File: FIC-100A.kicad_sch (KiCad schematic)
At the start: 0 parts

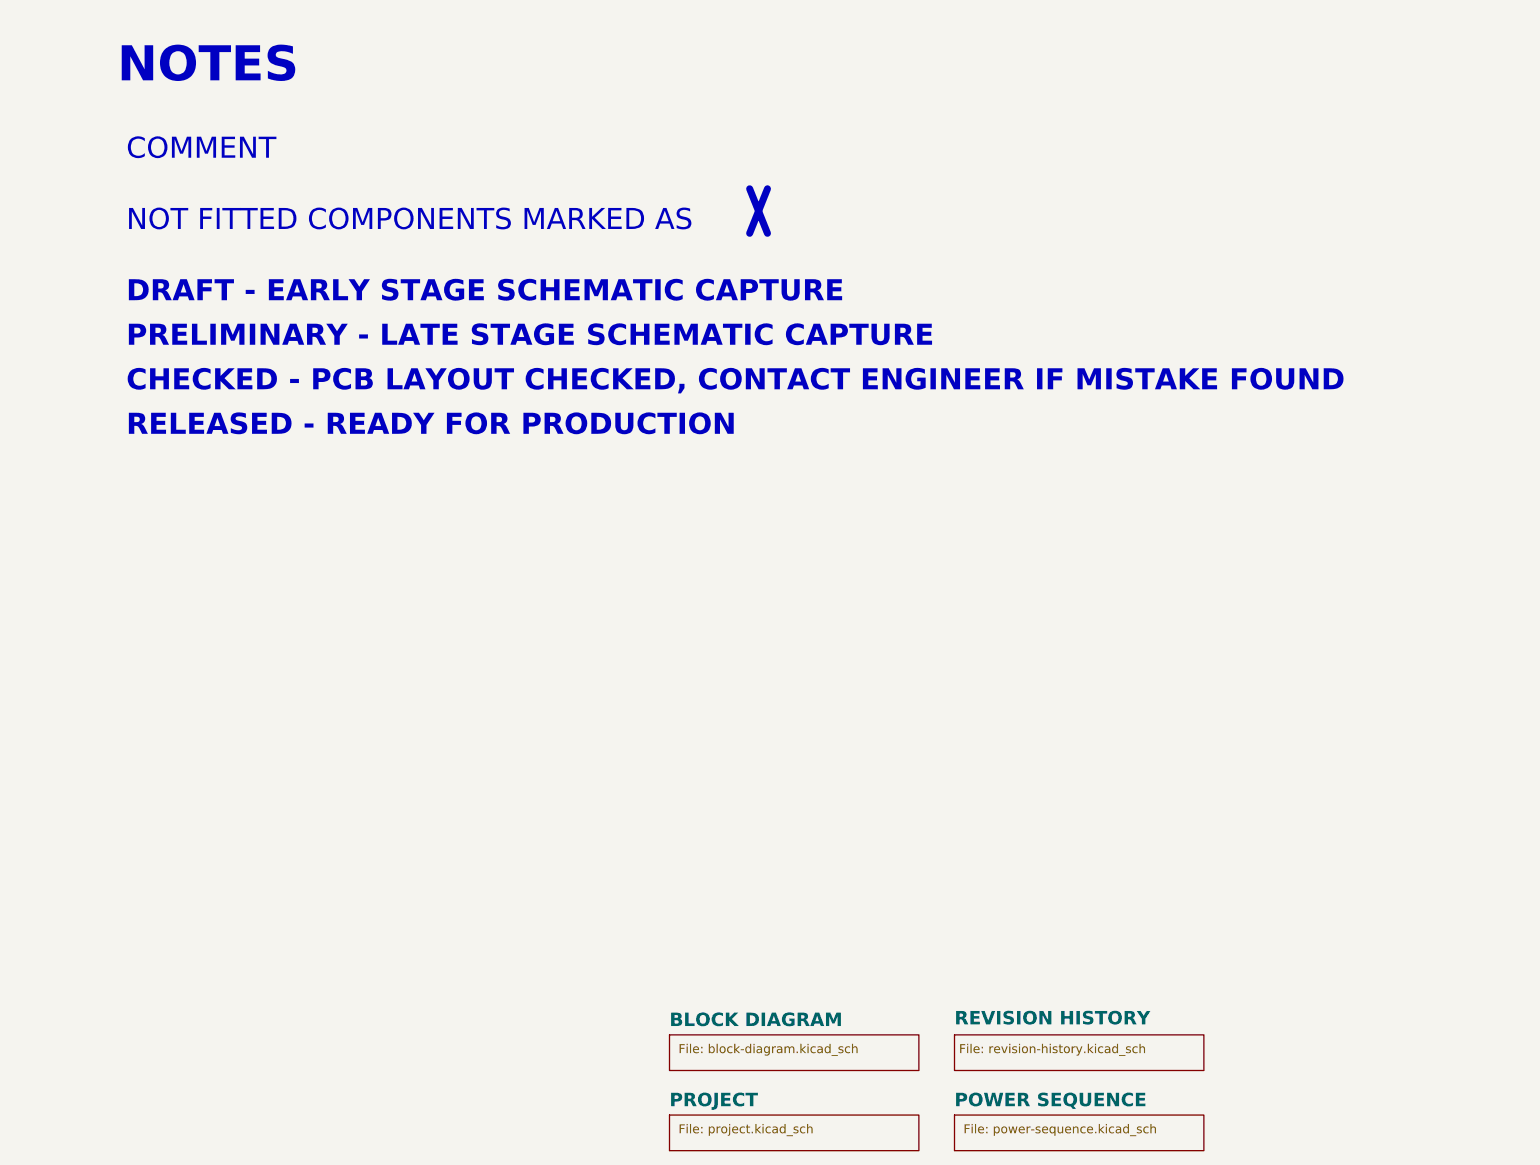
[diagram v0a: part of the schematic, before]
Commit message: test: exercise boardwright preview path
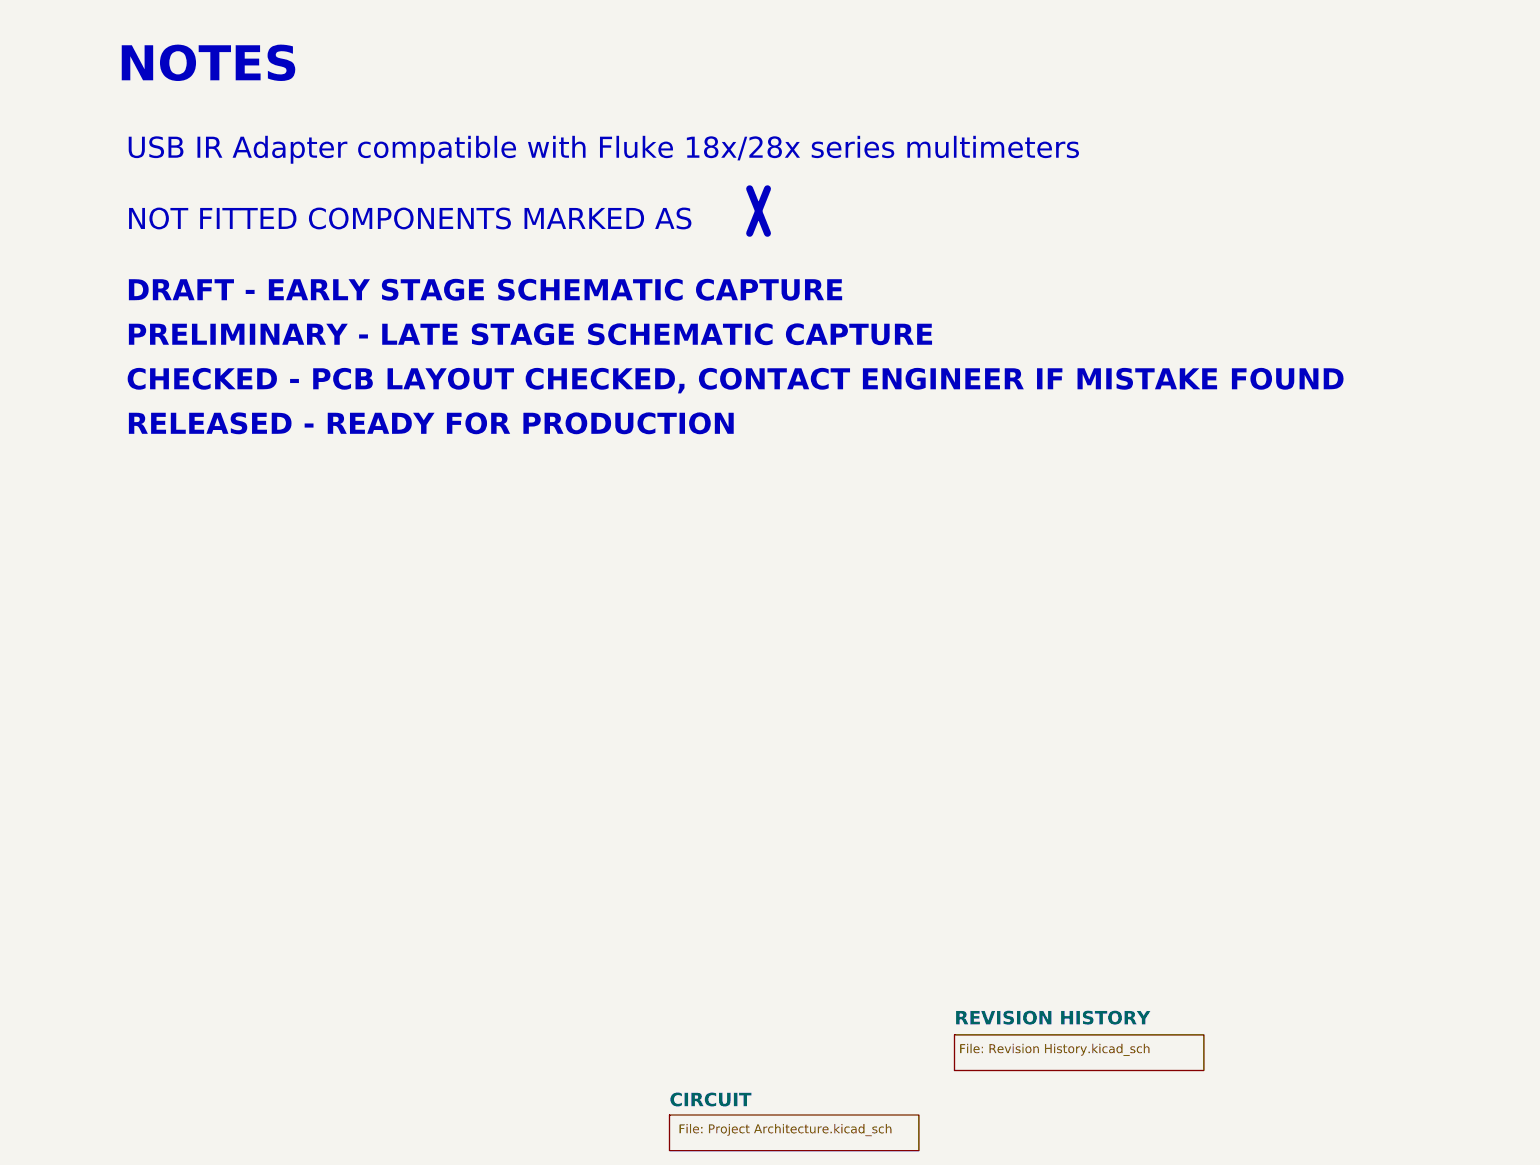
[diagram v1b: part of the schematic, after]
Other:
- sheet PROJECT renamed CIRCUIT
- removed sheet BLOCK DIAGRAM
- removed sheet POWER SEQUENCE
- sheet CIRCUIT: file project.kicad_sch -> Project Architecture.kicad_sch
- sheet REVISION HISTORY: file revision-history.kicad_sch -> Revision History.kicad_sch
- note added: "USB IR Adapter compatible with Fluke 18x/28x series multimeters"
- note removed: "COMMENT"
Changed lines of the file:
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@@
 	(paper "A3")
 	(title_block
-		(date "2025-01-12")
+		(date "2026-04-24")
 		(rev "${REVISION}")
 		(company "${COMPANY}")
@@
 		)
 	)
-	(text "COMMENT"
+	(text "USB IR Adapter compatible with Fluke 18x/28x series multimeters"
 		(exclude_from_sim no)
 		(at 222.25 177.8 0)
@@
 			(type dot)
 			(color 0 0 0 1)
-		)
-	)
-	(sheet
-		(at 340.36 313.69)
-		(size 35.56 5.08)
-		(exclude_from_sim no)
-		(in_bom yes)
-		(on_board yes)
-		(dnp no)
-		(stroke
-			(width 0.1524)
-			(type solid)
-		)
-		(fill
-			(color 0 0 0 0.0000)
-		)
-		(property "Sheetname" "POWER SEQUENCE"
-			(at 340.36 312.6609 0)
-			(effects
-				(font
-					(face "Times New Roman")
-					(size 1.905 1.905)
-					(bold yes)
-					(color 0 0 0 1)
-				)
-				(justify left bottom)
-			)
-		)
-		(property "Sheetfile" "power-sequence.kicad_sch"
-			(at 341.63 314.96 0)
-			(effects
-				(font
-					(face "Arial")
-					(size 1.27 1.27)
-				)
-				(justify left top)
-			)
-		)
-		(instances
-			(project "boardwright"
-				(path "/f9e05184-c88b-4a88-ae9c-ab2bdb32be7c"
-					(page "6")
-				)
-			)
 		)
 	)
@@
 			)
 		)
-		(property "Sheetfile" "revision-history.kicad_sch"
+		(property "Sheetfile" "Revision History.kicad_sch"
 			(at 340.995 303.53 0)
 			(effects
@@
 		)
 		(instances
-			(project "boardwright"
+			(project "FIC-100A"
 				(path "/f9e05184-c88b-4a88-ae9c-ab2bdb32be7c"
 					(page "7")
@@
 	)
 	(sheet
-		(at 299.72 302.26)
+		(at 299.72 313.69)
 		(size 35.56 5.08)
 		(exclude_from_sim no)
@@
 			(color 0 0 0 0.0000)
 		)
-		(property "Sheetname" "BLOCK DIAGRAM"
-			(at 299.72 301.2309 0)
-			(effects
-				(font
-					(face "Times New Roman")
-					(size 1.905 1.905)
-					(bold yes)
-					(color 0 0 0 1)
-				)
-				(justify left bottom)
-			)
-		)
-		(property "Sheetfile" "block-diagram.kicad_sch"
-			(at 300.99 303.53 0)
-			(effects
-				(font
-					(face "Arial")
-					(size 1.27 1.27)
-				)
-				(justify left top)
-			)
-		)
-		(instances
-			(project "boardwright"
-				(path "/f9e05184-c88b-4a88-ae9c-ab2bdb32be7c"
-					(page "2")
-				)
-			)
-		)
-	)
-	(sheet
-		(at 299.72 313.69)
-		(size 35.56 5.08)
-		(exclude_from_sim no)
-		(in_bom yes)
-		(on_board yes)
-		(dnp no)
-		(stroke
-			(width 0.1524)
-			(type solid)
-		)
-		(fill
-			(color 0 0 0 0.0000)
-		)
-		(property "Sheetname" "PROJECT"
+		(property "Sheetname" "CIRCUIT"
 			(at 299.72 312.6609 0)
 			(effects
@@
 			)
 		)
-		(property "Sheetfile" "project.kicad_sch"
+		(property "Sheetfile" "Project Architecture.kicad_sch"
 			(at 300.99 314.96 0)
 			(effects
@@
 		)
 		(instances
-			(project "boardwright"
+			(project "FIC-100A"
 				(path "/f9e05184-c88b-4a88-ae9c-ab2bdb32be7c"
 					(page "3")
